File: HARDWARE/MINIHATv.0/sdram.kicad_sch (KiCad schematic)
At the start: 8 parts, among them U5 IS42S16400N

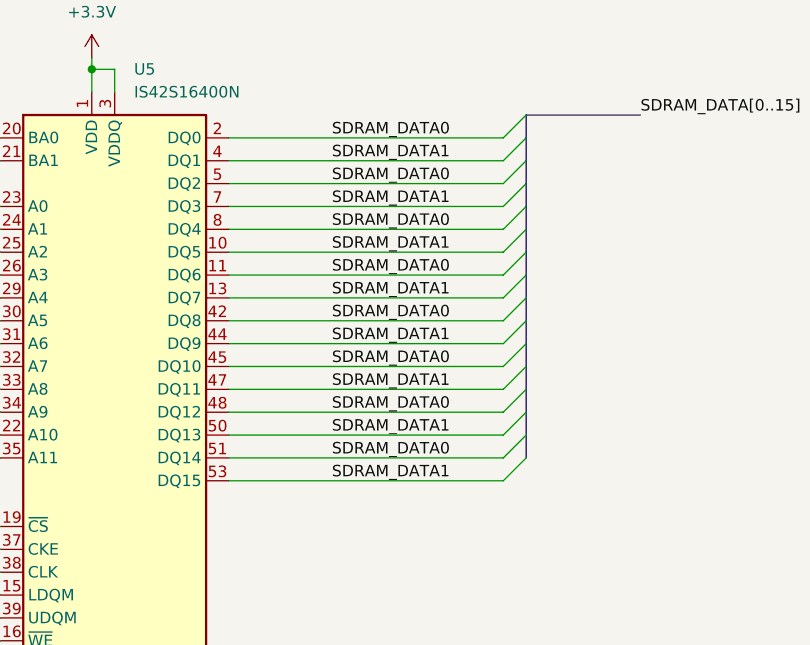
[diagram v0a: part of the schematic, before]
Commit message: added termination resistors , fixed data bus texts
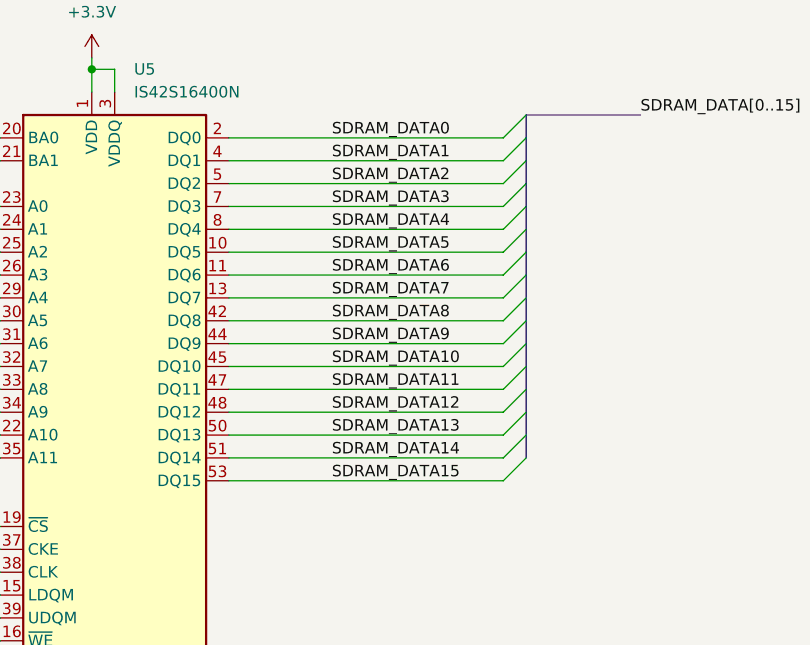
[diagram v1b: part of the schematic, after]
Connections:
- net SDRAM_DATA0: no longer U5.11 (DQ6), U5.42 (DQ8), U5.45 (DQ10), U5.48 (DQ12), U5.5 (DQ2), U5.51 (DQ14), U5.8 (DQ4)
- net SDRAM_DATA1: no longer U5.10 (DQ5), U5.13 (DQ7), U5.44 (DQ9), U5.47 (DQ11), U5.50 (DQ13), U5.53 (DQ15), U5.7 (DQ3)
- new net SDRAM_DATA10: U5.45 (DQ10)
- new net SDRAM_DATA11: U5.47 (DQ11)
- new net SDRAM_DATA12: U5.48 (DQ12)
- new net SDRAM_DATA13: U5.50 (DQ13)
- new net SDRAM_DATA14: U5.51 (DQ14)
- new net SDRAM_DATA15: U5.53 (DQ15)
- new net SDRAM_DATA2: U5.5 (DQ2)
- new net SDRAM_DATA3: U5.7 (DQ3)
- new net SDRAM_DATA4: U5.8 (DQ4)
- new net SDRAM_DATA5: U5.10 (DQ5)
- new net SDRAM_DATA6: U5.11 (DQ6)
- new net SDRAM_DATA7: U5.13 (DQ7)
- new net SDRAM_DATA8: U5.42 (DQ8)
- new net SDRAM_DATA9: U5.44 (DQ9)
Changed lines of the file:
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@@
 		)
 	)
-	(label "SDRAM_DATA1"
+	(label "SDRAM_DATA5"
 		(at 156.21 67.31 0)
 		(effects
@@
 		)
 	)
-	(label "SDRAM_DATA1"
+	(label "SDRAM_DATA9"
 		(at 156.21 77.47 0)
 		(effects
@@
 		)
 	)
-	(label "SDRAM_DATA0"
+	(label "SDRAM_DATA6"
 		(at 156.21 69.85 0)
 		(effects
@@
 		)
 	)
-	(label "SDRAM_DATA0"
+	(label "SDRAM_DATA12"
 		(at 156.21 85.09 0)
 		(effects
@@
 		)
 	)
-	(label "SDRAM_DATA0"
+	(label "SDRAM_DATA14"
 		(at 156.21 90.17 0)
 		(effects
@@
 		)
 	)
-	(label "SDRAM_DATA1"
+	(label "SDRAM_DATA3"
 		(at 156.21 62.23 0)
 		(effects
@@
 		)
 	)
-	(label "SDRAM_DATA0"
+	(label "SDRAM_DATA8"
 		(at 156.21 74.93 0)
 		(effects
@@
 		)
 	)
-	(label "SDRAM_DATA0"
+	(label "SDRAM_DATA10"
 		(at 156.21 80.01 0)
 		(effects
@@
 		)
 	)
-	(label "SDRAM_DATA1"
+	(label "SDRAM_DATA15"
 		(at 156.21 92.71 0)
 		(effects
@@
 		)
 	)
-	(label "SDRAM_DATA1"
+	(label "SDRAM_DATA11"
 		(at 156.21 82.55 0)
 		(effects
@@
 		)
 	)
-	(label "SDRAM_DATA0"
+	(label "SDRAM_DATA2"
 		(at 156.21 59.69 0)
 		(effects
@@
 		)
 	)
-	(label "SDRAM_DATA1"
+	(label "SDRAM_DATA13"
 		(at 156.21 87.63 0)
 		(effects
@@
 		)
 	)
-	(label "SDRAM_DATA0"
+	(label "SDRAM_DATA4"
 		(at 156.21 64.77 0)
 		(effects
@@
 		)
 	)
-	(label "SDRAM_DATA1"
+	(label "SDRAM_DATA7"
 		(at 156.21 72.39 0)
 		(effects

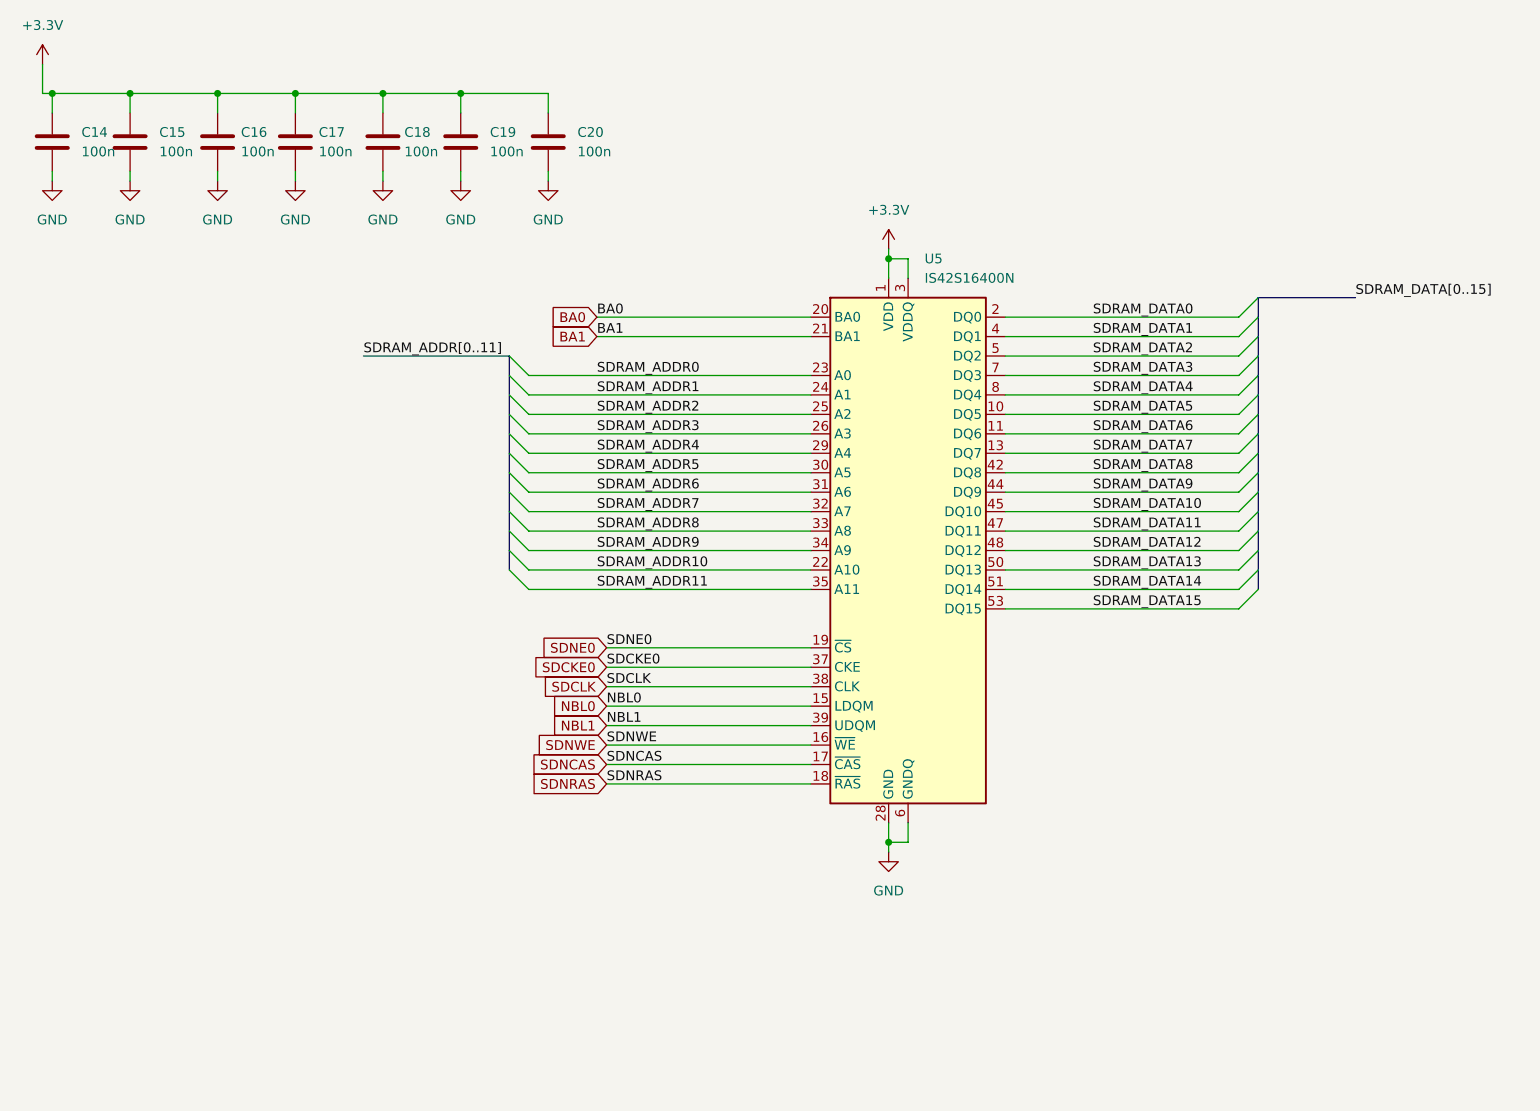
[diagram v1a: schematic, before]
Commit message: added normal buses
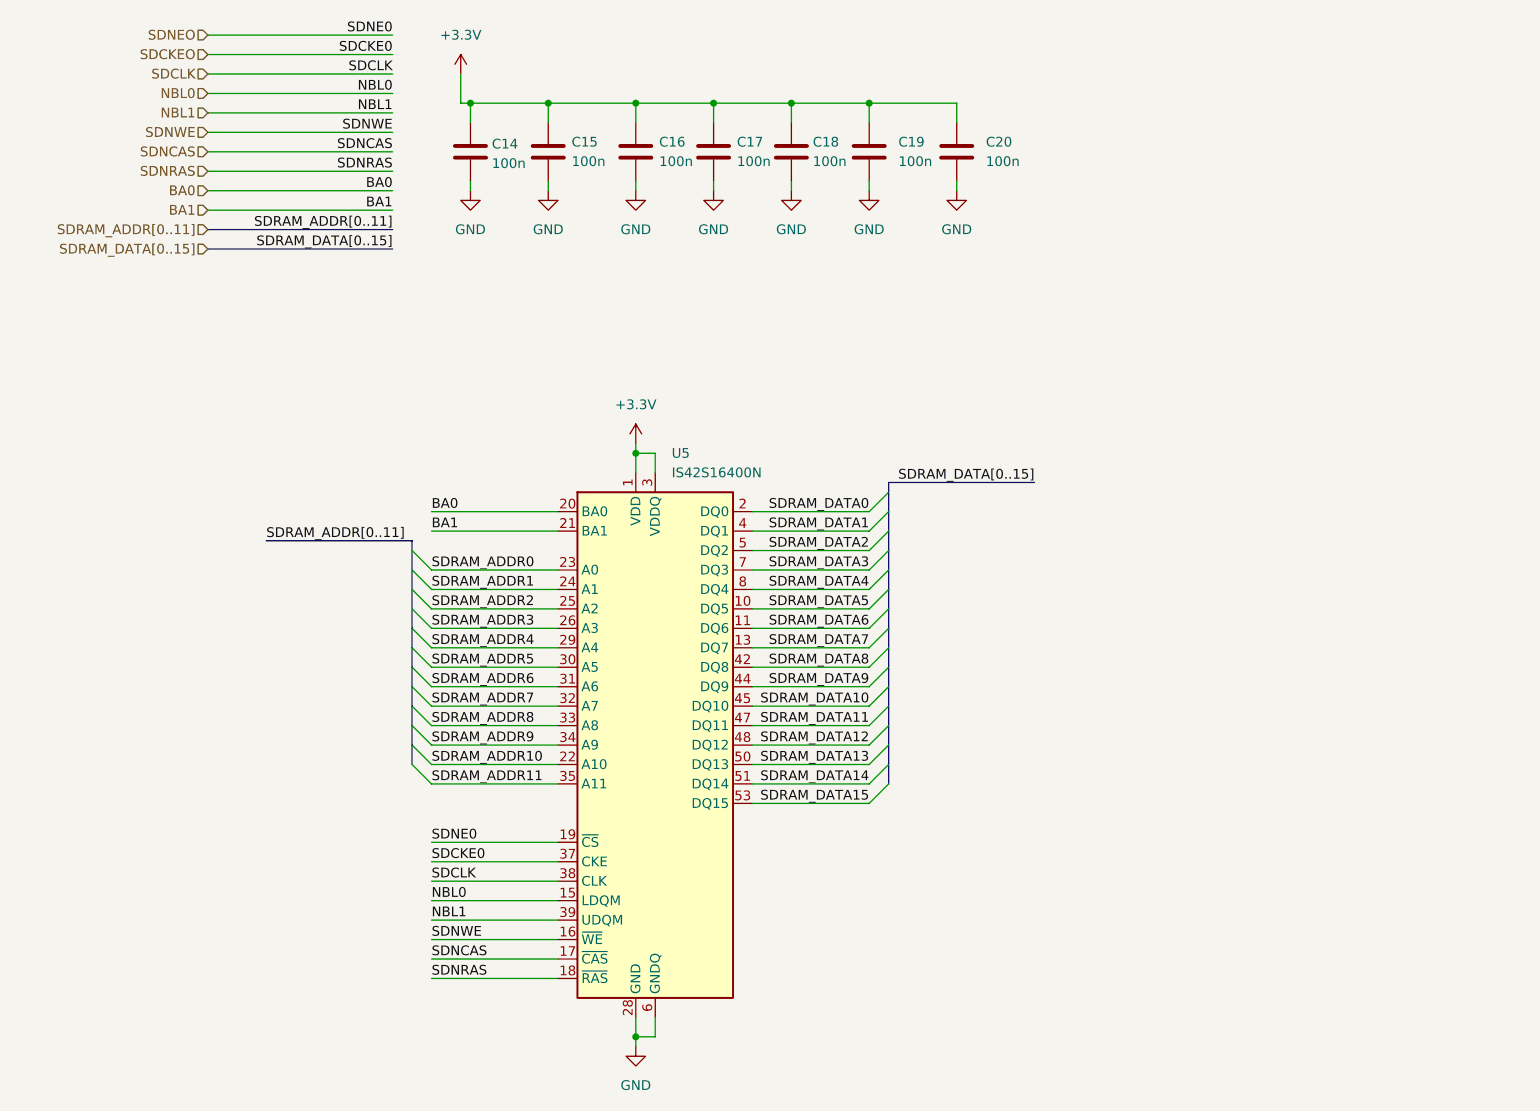
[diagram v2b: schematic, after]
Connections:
- net SDCKE0 renamed SDCKEO
- net SDNE0 renamed SDNEO
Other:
- moved on the sheet: C14, C15, C16, C17, C18, C19, C20, U5

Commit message: added sdram and usb pages to top page
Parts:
- renumbered C14 to C52, C15 to C53, C16 to C54, C17 to C55, C18 to C56, C19 to C57, C20 to C58, U5 to U9
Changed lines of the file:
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@@
 		(instances
 			(project "MINIHATv.0"
-				(path "/19041ef4-1d16-4363-8780-721ad9f20b33/93ff1453-7ee4-4ec9-9098-ce3a6e40c065"
+				(path "/19041ef4-1d16-4363-8780-721ad9f20b33/651dfc6f-3708-4c33-8923-f03a9f00fb7f"
 					(reference "#PWR042")
 					(unit 1)
@@
 		(in_pos_files yes)
 		(dnp no)
-		(property "Reference" "C17"
+		(property "Reference" "C55"
 			(at 109.728 31.75 0)
 			(show_name no)
@@
 		(instances
 			(project "MINIHATv.0"
-				(path "/19041ef4-1d16-4363-8780-721ad9f20b33/93ff1453-7ee4-4ec9-9098-ce3a6e40c065"
-					(reference "C17")
+				(path "/19041ef4-1d16-4363-8780-721ad9f20b33/651dfc6f-3708-4c33-8923-f03a9f00fb7f"
+					(reference "C55")
 					(unit 1)
 				)
@@
 		(instances
 			(project "MINIHATv.0"
-				(path "/19041ef4-1d16-4363-8780-721ad9f20b33/93ff1453-7ee4-4ec9-9098-ce3a6e40c065"
+				(path "/19041ef4-1d16-4363-8780-721ad9f20b33/651dfc6f-3708-4c33-8923-f03a9f00fb7f"
 					(reference "#PWR046")
 					(unit 1)
@@
 		(dnp no)
 		(fields_autoplaced yes)
-		(property "Reference" "C20"
+		(property "Reference" "C58"
 			(at 142.24 31.7499 0)
 			(show_name no)
@@
 		(instances
 			(project "MINIHATv.0"
-				(path "/19041ef4-1d16-4363-8780-721ad9f20b33/93ff1453-7ee4-4ec9-9098-ce3a6e40c065"
-					(reference "C20")
+				(path "/19041ef4-1d16-4363-8780-721ad9f20b33/651dfc6f-3708-4c33-8923-f03a9f00fb7f"
+					(reference "C58")
 					(unit 1)
 				)
@@
 		(instances
 			(project "MINIHATv.0"
-				(path "/19041ef4-1d16-4363-8780-721ad9f20b33/93ff1453-7ee4-4ec9-9098-ce3a6e40c065"
+				(path "/19041ef4-1d16-4363-8780-721ad9f20b33/651dfc6f-3708-4c33-8923-f03a9f00fb7f"
 					(reference "#PWR043")
 					(unit 1)
@@
 		(instances
 			(project "MINIHATv.0"
-				(path "/19041ef4-1d16-4363-8780-721ad9f20b33/93ff1453-7ee4-4ec9-9098-ce3a6e40c065"
+				(path "/19041ef4-1d16-4363-8780-721ad9f20b33/651dfc6f-3708-4c33-8923-f03a9f00fb7f"
 					(reference "#PWR048")
 					(unit 1)
@@
 		(dnp no)
 		(fields_autoplaced yes)
-		(property "Reference" "C19"
+		(property "Reference" "C57"
 			(at 130.81 31.7499 0)
 			(show_name no)
@@
 		(instances
 			(project "MINIHATv.0"
-				(path "/19041ef4-1d16-4363-8780-721ad9f20b33/93ff1453-7ee4-4ec9-9098-ce3a6e40c065"
-					(reference "C19")
+				(path "/19041ef4-1d16-4363-8780-721ad9f20b33/651dfc6f-3708-4c33-8923-f03a9f00fb7f"
+					(reference "C57")
 					(unit 1)
 				)
@@
 		(in_pos_files yes)
 		(dnp no)
-		(property "Reference" "C16"
+		(property "Reference" "C54"
 			(at 99.568 31.75 0)
 			(show_name no)
@@
 		(instances
 			(project "MINIHATv.0"
-				(path "/19041ef4-1d16-4363-8780-721ad9f20b33/93ff1453-7ee4-4ec9-9098-ce3a6e40c065"
-					(reference "C16")
+				(path "/19041ef4-1d16-4363-8780-721ad9f20b33/651dfc6f-3708-4c33-8923-f03a9f00fb7f"
+					(reference "C54")
 					(unit 1)
 				)
@@
 		(instances
 			(project "MINIHATv.0"
-				(path "/19041ef4-1d16-4363-8780-721ad9f20b33/93ff1453-7ee4-4ec9-9098-ce3a6e40c065"
+				(path "/19041ef4-1d16-4363-8780-721ad9f20b33/651dfc6f-3708-4c33-8923-f03a9f00fb7f"
 					(reference "#PWR047")
 					(unit 1)
@@
 		(instances
 			(project "MINIHATv.0"
-				(path "/19041ef4-1d16-4363-8780-721ad9f20b33/93ff1453-7ee4-4ec9-9098-ce3a6e40c065"
+				(path "/19041ef4-1d16-4363-8780-721ad9f20b33/651dfc6f-3708-4c33-8923-f03a9f00fb7f"
 					(reference "#PWR049")
 					(unit 1)
@@
 		(instances
 			(project "MINIHATv.0"
-				(path "/19041ef4-1d16-4363-8780-721ad9f20b33/93ff1453-7ee4-4ec9-9098-ce3a6e40c065"
+				(path "/19041ef4-1d16-4363-8780-721ad9f20b33/651dfc6f-3708-4c33-8923-f03a9f00fb7f"
 					(reference "#PWR050")
 					(unit 1)
@@
 		(in_pos_files yes)
 		(dnp no)
-		(property "Reference" "C14"
+		(property "Reference" "C52"
 			(at 77.724 32.004 0)
 			(show_name no)
@@
 		(instances
 			(project "MINIHATv.0"
-				(path "/19041ef4-1d16-4363-8780-721ad9f20b33/93ff1453-7ee4-4ec9-9098-ce3a6e40c065"
-					(reference "C14")
+				(path "/19041ef4-1d16-4363-8780-721ad9f20b33/651dfc6f-3708-4c33-8923-f03a9f00fb7f"
+					(reference "C52")
 					(unit 1)
 				)
@@
 		(instances
 			(project "MINIHATv.0"
-				(path "/19041ef4-1d16-4363-8780-721ad9f20b33/93ff1453-7ee4-4ec9-9098-ce3a6e40c065"
+				(path "/19041ef4-1d16-4363-8780-721ad9f20b33/651dfc6f-3708-4c33-8923-f03a9f00fb7f"
 					(reference "#PWR045")
 					(unit 1)
@@
 		(in_pos_files yes)
 		(dnp no)
-		(property "Reference" "C18"
+		(property "Reference" "C56"
 			(at 119.634 31.75 0)
 			(show_name no)
@@
 		(instances
 			(project "MINIHATv.0"
-				(path "/19041ef4-1d16-4363-8780-721ad9f20b33/93ff1453-7ee4-4ec9-9098-ce3a6e40c065"
-					(reference "C18")
+				(path "/19041ef4-1d16-4363-8780-721ad9f20b33/651dfc6f-3708-4c33-8923-f03a9f00fb7f"
+					(reference "C56")
 					(unit 1)
 				)
@@
 		(instances
 			(project "MINIHATv.0"
-				(path "/19041ef4-1d16-4363-8780-721ad9f20b33/93ff1453-7ee4-4ec9-9098-ce3a6e40c065"
+				(path "/19041ef4-1d16-4363-8780-721ad9f20b33/651dfc6f-3708-4c33-8923-f03a9f00fb7f"
 					(reference "#PWR051")
 					(unit 1)
@@
 		(in_pos_files yes)
 		(dnp no)
-		(property "Reference" "C15"
+		(property "Reference" "C53"
 			(at 88.138 31.75 0)
 			(show_name no)
@@
 		(instances
 			(project "MINIHATv.0"
-				(path "/19041ef4-1d16-4363-8780-721ad9f20b33/93ff1453-7ee4-4ec9-9098-ce3a6e40c065"
-					(reference "C15")
+				(path "/19041ef4-1d16-4363-8780-721ad9f20b33/651dfc6f-3708-4c33-8923-f03a9f00fb7f"
+					(reference "C53")
 					(unit 1)
 				)
@@
 		(dnp no)
 		(fields_autoplaced yes)
-		(property "Reference" "U5"
+		(property "Reference" "U9"
 			(at 101.2033 72.39 0)
 			(show_name no)
@@
 		(instances
 			(project "MINIHATv.0"
-				(path "/19041ef4-1d16-4363-8780-721ad9f20b33/93ff1453-7ee4-4ec9-9098-ce3a6e40c065"
-					(reference "U5")
+				(path "/19041ef4-1d16-4363-8780-721ad9f20b33/651dfc6f-3708-4c33-8923-f03a9f00fb7f"
+					(reference "U9")
 					(unit 1)
 				)
@@
 		(instances
 			(project "MINIHATv.0"
-				(path "/19041ef4-1d16-4363-8780-721ad9f20b33/93ff1453-7ee4-4ec9-9098-ce3a6e40c065"
+				(path "/19041ef4-1d16-4363-8780-721ad9f20b33/651dfc6f-3708-4c33-8923-f03a9f00fb7f"
 					(reference "#PWR044")
 					(unit 1)
